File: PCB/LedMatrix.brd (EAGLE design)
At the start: 32 x 34 mm, 12 parts, among them IC1 74HC164D

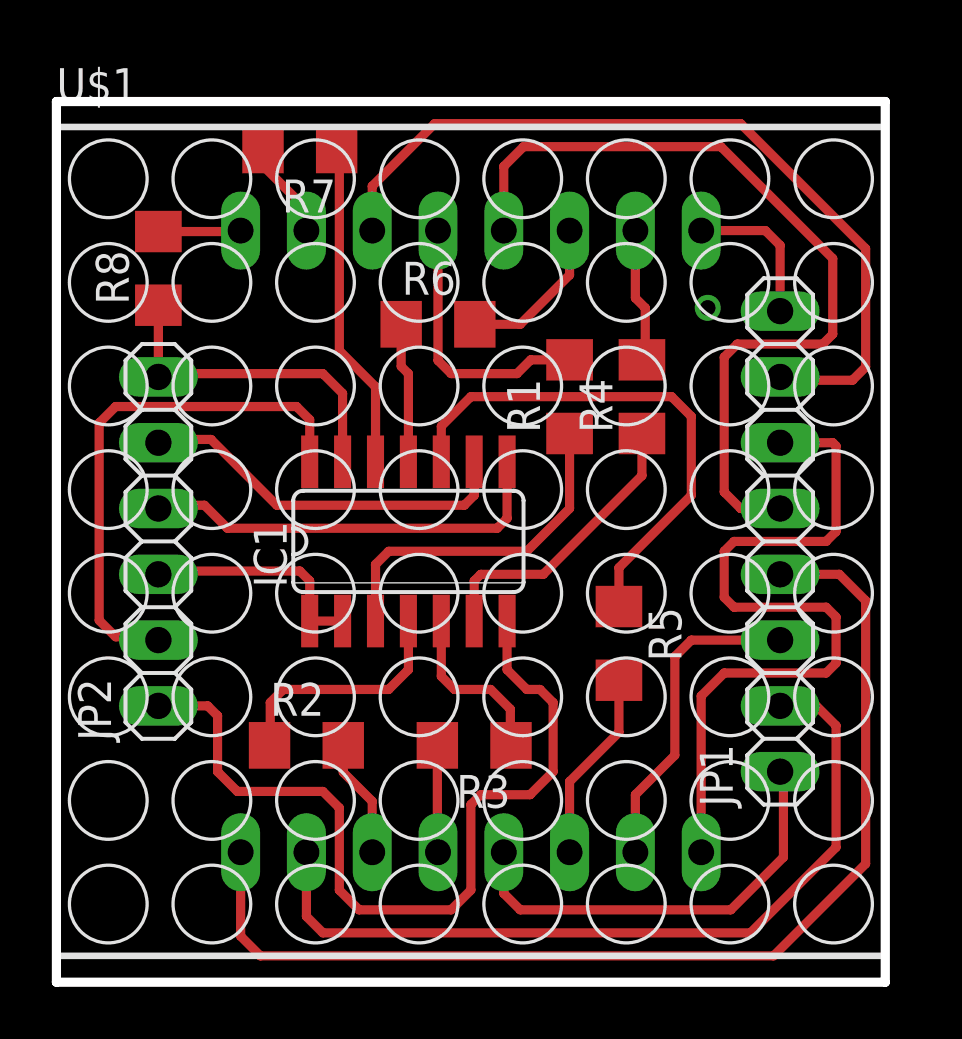
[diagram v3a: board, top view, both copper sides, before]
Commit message: Another part of improvements in pcb layouts. Especially in pinhead area, to match both pcbs.
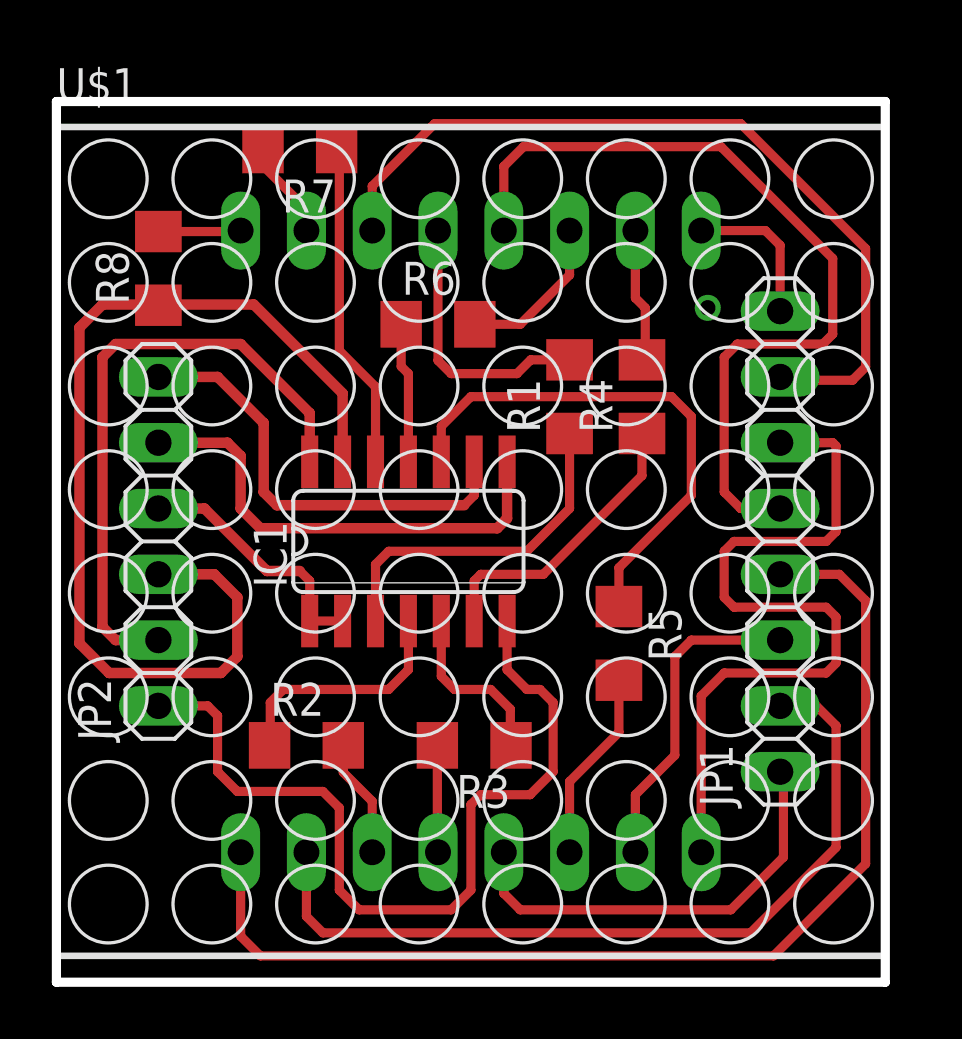
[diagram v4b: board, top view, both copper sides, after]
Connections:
- net N$16: now also JP2.3; no longer JP2.6
- net N$26: now also JP2.6; no longer JP2.5
- net N$27: now also JP2.5; no longer JP2.4
- net N$28: now also JP2.4; no longer JP2.3
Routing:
- net N$16: track 12.9 -> 39.3 mm
- net VCC: track 20.4 -> 24.0 mm
- net N$26: track 14.7 -> 17.3 mm
- net N$27: track 16.2 -> 18.4 mm
- net N$28: track 8.87 -> 9.82 mm
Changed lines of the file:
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@@
 <contactref element="IC1" pad="14"/>
 <contactref element="JP2" pad="2"/>
-<wire x1="9.271" y1="22.225" x2="2.286" y2="22.225" width="0.3556" layer="1"/>
-<wire x1="2.286" y1="13.335" x2="1.651" y2="13.97" width="0.3556" layer="1"/>
-<wire x1="1.651" y1="13.97" x2="1.651" y2="21.59" width="0.3556" layer="1"/>
-<wire x1="1.651" y1="21.59" x2="2.286" y2="22.225" width="0.3556" layer="1"/>
-<wire x1="9.779" y1="20.0914" x2="9.779" y2="21.717" width="0.3556" layer="1"/>
-<wire x1="9.779" y1="21.717" x2="9.271" y2="22.225" width="0.3556" layer="1"/>
-<wire x1="2.286" y1="13.335" x2="3.81" y2="13.335" width="0.3556" layer="1"/>
-<wire x1="3.81" y1="13.335" x2="3.937" y2="13.208" width="0.3556" layer="1"/>
+<wire x1="2.286" y1="24.638" x2="1.778" y2="24.13" width="0.4064" layer="1"/>
+<wire x1="1.778" y1="24.13" x2="1.778" y2="13.716" width="0.4064" layer="1"/>
+<wire x1="1.778" y1="13.716" x2="2.286" y2="13.208" width="0.4064" layer="1"/>
+<wire x1="2.286" y1="13.208" x2="3.937" y2="13.208" width="0.4064" layer="1"/>
+<wire x1="2.286" y1="24.638" x2="7.112" y2="24.638" width="0.4064" layer="1"/>
+<wire x1="7.112" y1="24.638" x2="9.779" y2="21.971" width="0.4064" layer="1"/>
+<wire x1="9.779" y1="21.971" x2="9.779" y2="20.0914" width="0.4064" layer="1"/>
 </signal>
 <signal name="N$1">
@@
 <contactref element="R8" pad="1"/>
 <contactref element="IC1" pad="13"/>
-<contactref element="JP2" pad="6"/>
-<wire x1="11.049" y1="20.0914" x2="11.049" y2="22.733" width="0.3556" layer="1"/>
-<wire x1="11.049" y1="22.733" x2="10.287" y2="23.495" width="0.3556" layer="1"/>
-<wire x1="10.287" y1="23.495" x2="4.064" y2="23.495" width="0.3556" layer="1"/>
-<wire x1="4.064" y1="23.495" x2="3.937" y2="23.368" width="0.3556" layer="1"/>
-<wire x1="3.937" y1="26.137" x2="3.937" y2="23.368" width="0.3556" layer="1"/>
+<contactref element="JP2" pad="3"/>
+<wire x1="11.049" y1="20.0914" x2="11.049" y2="22.733" width="0.4064" layer="1"/>
+<wire x1="11.049" y1="22.733" x2="7.62" y2="26.162" width="0.4064" layer="1"/>
+<wire x1="7.62" y1="26.162" x2="3.962" y2="26.162" width="0.4064" layer="1"/>
+<wire x1="3.962" y1="26.162" x2="3.937" y2="26.137" width="0.4064" layer="1"/>
+<wire x1="3.937" y1="15.748" x2="6.096" y2="15.748" width="0.4064" layer="1"/>
+<wire x1="6.096" y1="15.748" x2="6.985" y2="14.859" width="0.4064" layer="1"/>
+<wire x1="6.985" y1="14.859" x2="6.985" y2="12.573" width="0.4064" layer="1"/>
+<wire x1="6.985" y1="12.573" x2="6.35" y2="11.938" width="0.4064" layer="1"/>
+<wire x1="6.35" y1="11.938" x2="2.032" y2="11.938" width="0.4064" layer="1"/>
+<wire x1="2.032" y1="11.938" x2="0.889" y2="13.081" width="0.4064" layer="1"/>
+<wire x1="0.889" y1="13.081" x2="0.889" y2="25.273" width="0.4064" layer="1"/>
+<wire x1="0.889" y1="25.273" x2="1.778" y2="26.162" width="0.4064" layer="1"/>
+<wire x1="1.778" y1="26.162" x2="3.912" y2="26.162" width="0.4064" layer="1"/>
+<wire x1="3.912" y1="26.162" x2="3.937" y2="26.137" width="0.4064" layer="1"/>
 </signal>
 <signal name="N$17">
@@
 <contactref element="IC1" pad="2"/>
 <wire x1="11.049" y1="13.9446" x2="9.779" y2="13.9446" width="0.3556" layer="1"/>
-<contactref element="JP2" pad="3"/>
 <wire x1="9.398" y1="15.875" x2="9.779" y2="15.494" width="0.3556" layer="1"/>
 <wire x1="9.779" y1="15.494" x2="9.779" y2="13.9446" width="0.3556" layer="1"/>
-<wire x1="9.398" y1="15.875" x2="4.064" y2="15.875" width="0.3556" layer="1"/>
-<wire x1="4.064" y1="15.875" x2="3.937" y2="15.748" width="0.3556" layer="1"/>
-</signal>
-<signal name="N$27">
-<contactref element="IC1" pad="8"/>
-<wire x1="17.399" y1="20.0914" x2="17.399" y2="17.907" width="0.3556" layer="1"/>
-<wire x1="17.018" y1="17.526" x2="6.604" y2="17.526" width="0.3556" layer="1"/>
-<wire x1="17.399" y1="17.907" x2="17.018" y2="17.526" width="0.3556" layer="1"/>
 <contactref element="JP2" pad="4"/>
-<wire x1="5.715" y1="18.415" x2="6.604" y2="17.526" width="0.3556" layer="1"/>
-<wire x1="5.715" y1="18.415" x2="4.064" y2="18.415" width="0.3556" layer="1"/>
-<wire x1="4.064" y1="18.415" x2="3.937" y2="18.288" width="0.3556" layer="1"/>
+<wire x1="9.398" y1="15.875" x2="8.128" y2="15.875" width="0.4064" layer="1"/>
+<wire x1="8.128" y1="15.875" x2="5.715" y2="18.288" width="0.4064" layer="1"/>
+<wire x1="5.715" y1="18.288" x2="3.937" y2="18.288" width="0.4064" layer="1"/>
 </signal>
 <signal name="N$25">
@@
 <signal name="N$26">
 <contactref element="IC1" pad="9"/>
-<contactref element="JP2" pad="5"/>
 <wire x1="16.129" y1="20.0914" x2="16.129" y2="18.796" width="0.3556" layer="1"/>
 <wire x1="16.129" y1="18.796" x2="15.748" y2="18.415" width="0.3556" layer="1"/>
-<wire x1="15.748" y1="18.415" x2="8.509" y2="18.415" width="0.3556" layer="1"/>
-<wire x1="8.509" y1="18.415" x2="5.969" y2="20.955" width="0.3556" layer="1"/>
-<wire x1="5.969" y1="20.955" x2="4.064" y2="20.955" width="0.3556" layer="1"/>
-<wire x1="4.064" y1="20.955" x2="3.937" y2="20.828" width="0.3556" layer="1"/>
+<contactref element="JP2" pad="6"/>
+<wire x1="3.937" y1="23.368" x2="6.223" y2="23.368" width="0.4064" layer="1"/>
+<wire x1="6.223" y1="23.368" x2="8.001" y2="21.59" width="0.4064" layer="1"/>
+<wire x1="8.001" y1="21.59" x2="8.001" y2="18.923" width="0.4064" layer="1"/>
+<wire x1="8.001" y1="18.923" x2="8.509" y2="18.415" width="0.4064" layer="1"/>
+<wire x1="8.509" y1="18.415" x2="15.748" y2="18.415" width="0.4064" layer="1"/>
+</signal>
+<signal name="N$27">
+<contactref element="JP2" pad="5"/>
+<contactref element="IC1" pad="8"/>
+<wire x1="17.399" y1="20.0914" x2="17.399" y2="17.907" width="0.4064" layer="1"/>
+<wire x1="17.399" y1="17.907" x2="17.018" y2="17.526" width="0.4064" layer="1"/>
+<wire x1="17.018" y1="17.526" x2="7.874" y2="17.526" width="0.4064" layer="1"/>
+<wire x1="7.874" y1="17.526" x2="7.112" y2="18.288" width="0.4064" layer="1"/>
+<wire x1="7.112" y1="18.288" x2="7.112" y2="20.32" width="0.4064" layer="1"/>
+<wire x1="7.112" y1="20.32" x2="6.604" y2="20.828" width="0.4064" layer="1"/>
+<wire x1="6.604" y1="20.828" x2="3.937" y2="20.828" width="0.4064" layer="1"/>
 </signal>
 </signals>

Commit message: Added descriptions to the lines on the ledMatrix board.
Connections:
- net N$16 renamed OUTPUT
- net N$17 renamed COL1
- net N$18 renamed COL2
- net N$19 renamed COL3
- net N$20 renamed COL4
- net N$21 renamed COL5
- net N$22 renamed COL6
- net N$23 renamed COL7
- net N$24 renamed COL8
- net N$26 renamed CLR
- net N$27 renamed CLK
- net N$28 renamed INPUT
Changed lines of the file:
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@@
 <wire x1="12.319" y1="22.987" x2="10.922" y2="24.384" width="0.3556" layer="1"/>
 </signal>
-<signal name="N$16">
+<signal name="OUTPUT">
 <contactref element="R8" pad="1"/>
 <contactref element="IC1" pad="13"/>
@@
 <wire x1="3.912" y1="26.162" x2="3.937" y2="26.137" width="0.4064" layer="1"/>
 </signal>
-<signal name="N$17">
+<signal name="COL1">
 <contactref element="JP1" pad="8"/>
 <contactref element="U$1" pad="9"/>
@@
 <wire x1="27.94" y1="28.448" x2="27.94" y2="25.908" width="0.3556" layer="1"/>
 </signal>
-<signal name="N$18">
+<signal name="COL2">
 <contactref element="JP1" pad="7"/>
 <contactref element="U$1" pad="14"/>
@@
 <wire x1="26.416" y1="33.147" x2="14.605" y2="33.147" width="0.3556" layer="1"/>
 </signal>
-<signal name="N$19">
+<signal name="COL3">
 <contactref element="JP1" pad="6"/>
 <contactref element="U$1" pad="8"/>
@@
 <wire x1="29.972" y1="20.828" x2="30.099" y2="20.701" width="0.3556" layer="1"/>
 </signal>
-<signal name="N$20">
+<signal name="COL4">
 <contactref element="JP1" pad="5"/>
 <contactref element="U$1" pad="12"/>
@@
 <wire x1="29.972" y1="27.94" x2="29.972" y2="25.019" width="0.3556" layer="1"/>
 </signal>
-<signal name="N$21">
+<signal name="COL5">
 <contactref element="JP1" pad="4"/>
 <contactref element="U$1" pad="1"/>
@@
 <wire x1="31.242" y1="14.732" x2="30.226" y2="15.748" width="0.3556" layer="1"/>
 </signal>
-<signal name="N$22">
+<signal name="COL6">
 <contactref element="JP1" pad="3"/>
 <contactref element="U$1" pad="7"/>
@@
 <wire x1="24.511" y1="13.208" x2="27.94" y2="13.208" width="0.3556" layer="1"/>
 </signal>
-<signal name="N$23">
+<signal name="COL7">
 <contactref element="JP1" pad="2"/>
 <contactref element="U$1" pad="2"/>
@@
 <wire x1="30.099" y1="9.906" x2="30.099" y2="5.207" width="0.3556" layer="1"/>
 </signal>
-<signal name="N$24">
+<signal name="COL8">
 <contactref element="JP1" pad="1"/>
 <contactref element="U$1" pad="5"/>
@@
 <wire x1="17.907" y1="2.794" x2="17.272" y2="3.429" width="0.3556" layer="1"/>
 </signal>
-<signal name="N$28">
+<signal name="INPUT">
 <contactref element="IC1" pad="1"/>
 <contactref element="IC1" pad="2"/>
@@
 <via x="25.146" y="26.035" extent="1-16" drill="0.6" shape="square"/>
 </signal>
-<signal name="N$26">
+<signal name="CLR">
 <contactref element="IC1" pad="9"/>
 <wire x1="16.129" y1="20.0914" x2="16.129" y2="18.796" width="0.3556" layer="1"/>
@@
 <wire x1="8.509" y1="18.415" x2="15.748" y2="18.415" width="0.4064" layer="1"/>
 </signal>
-<signal name="N$27">
+<signal name="CLK">
 <contactref element="JP2" pad="5"/>
 <contactref element="IC1" pad="8"/>
